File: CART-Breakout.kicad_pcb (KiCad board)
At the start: 2 copper layers, 47 x 50 mm, 11 parts, among them P1 CONN_01X05, P2 CONN_01X05, P3 CONN_01X05, P4 CONN_01X05, P5 CONN_01X05, P6 CONN_01X05

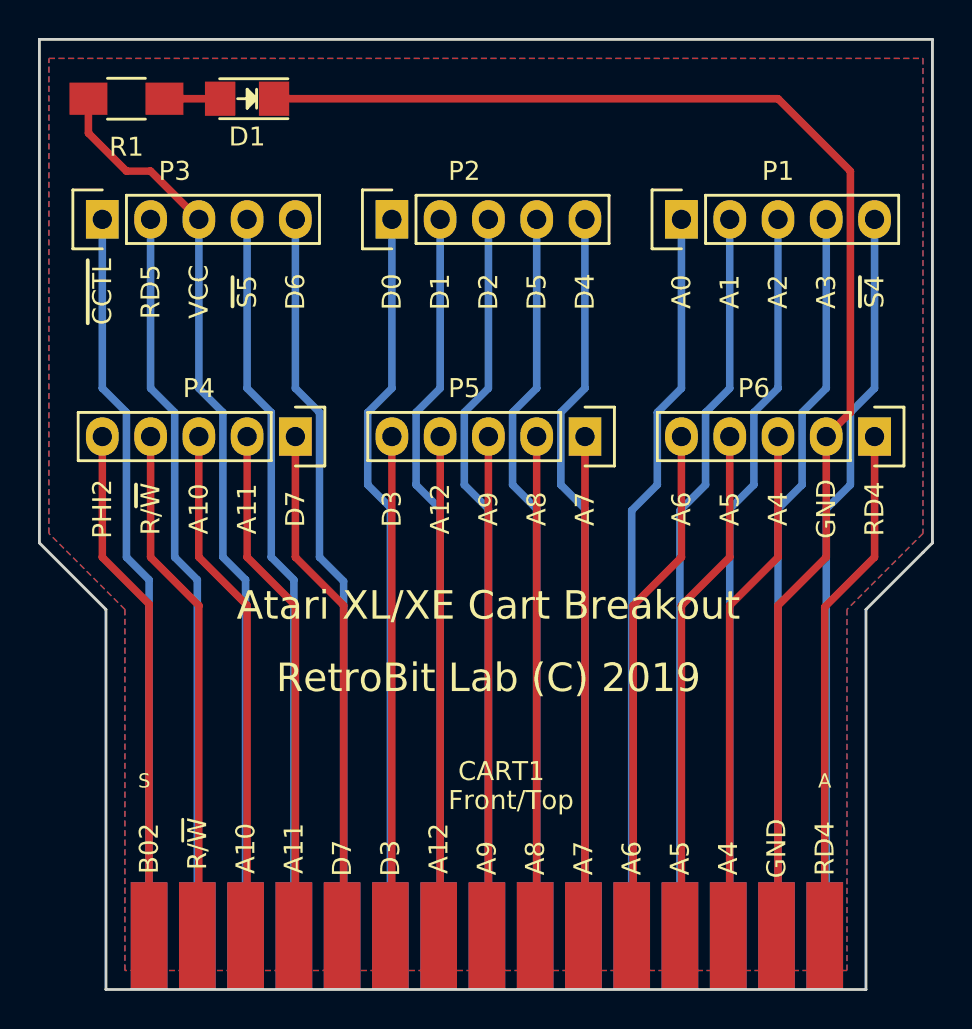
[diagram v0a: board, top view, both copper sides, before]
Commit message: Updated from KiCAD 4 to KiCAD 5.1.19
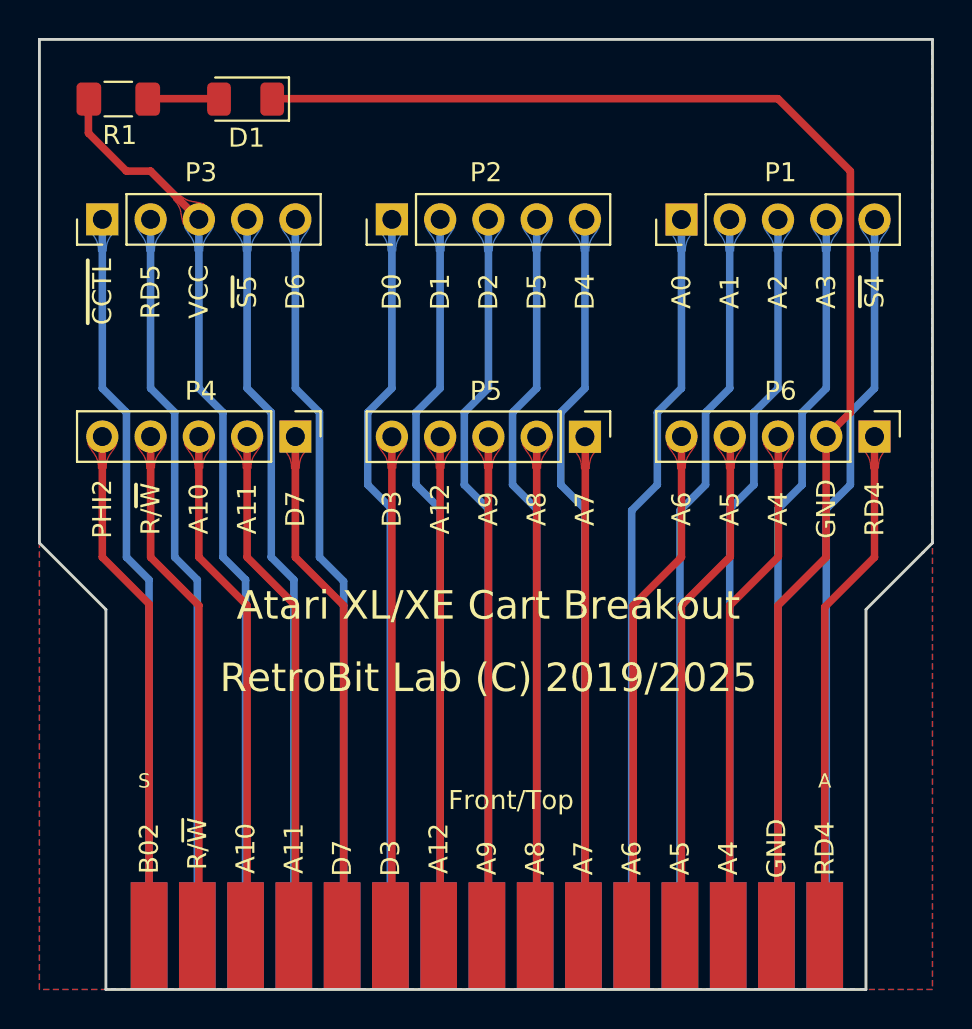
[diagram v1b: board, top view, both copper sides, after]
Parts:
- removed LOGO: KiCad-Logo_5mm_SilkScreen, Symbol:KiCad-Logo_5mm_SilkScreen
- removed OSHW: OSHW-Logo_5.7x6mm_SilkScreen, Symbol:OSHW-Logo_5.7x6mm_SilkScreen
- added L1: LOGO, Symbol:OSHW-Logo2_7.3x6mm_SilkScreen, B.Cu at (151.5, 104.0)
- added L2: LOGO, Symbol:KiCad-Logo2_5mm_SilkScreen, B.Cu at (151.0, 97.5)
- D1: footprint LEDs:LED_1206 -> LED_SMD:LED_1206_3216Metric
- P1, P2, P3, P4, P5, P6: value CONN_01X05 -> Conn_01x05; footprint Pin_Headers:Pin_Header_Straight_1x05 -> Connector_PinHeader_2.54mm:PinHeader_1x05_P2.54mm_Vertical
- R1: footprint Resistors_SMD:R_1206_HandSoldering -> Resistor_SMD:R_1206_3216Metric_Pad1.30x1.75mm_HandSolder
- moved R1 0.43 mm to (131.7, 71.1)
- moved D1 0.08 mm to (138.3, 71.1)
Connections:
- net Net-(CART1-Pad1) renamed /~S4
- net Net-(CART1-Pad10) renamed /D0
- net Net-(CART1-Pad11) renamed /D6
- net Net-(CART1-Pad12) renamed /~S5
- net Net-(CART1-Pad14) renamed /RD5
- net Net-(CART1-Pad15) renamed /~CCTL
- net Net-(CART1-Pad2) renamed /A3
- net Net-(CART1-Pad3) renamed /A2
- net Net-(CART1-Pad4) renamed /A1
- net Net-(CART1-Pad5) renamed /A0
- net Net-(CART1-Pad6) renamed /D4
- net Net-(CART1-Pad7) renamed /D5
- net Net-(CART1-Pad8) renamed /D2
- net Net-(CART1-Pad9) renamed /D1
- net Net-(CART1-PadA) renamed /RD4
- net Net-(CART1-PadC) renamed /A4
- net Net-(CART1-PadD) renamed /A5
- net Net-(CART1-PadE) renamed /A6
- net Net-(CART1-PadF) renamed /A7
- net Net-(CART1-PadH) renamed /A8
- net Net-(CART1-PadJ) renamed /A9
- net Net-(CART1-PadK) renamed /A12
- net Net-(CART1-PadL) renamed /D3
- net Net-(CART1-PadM) renamed /D7
- net Net-(CART1-PadN) renamed /A11
- net Net-(CART1-PadP) renamed /A10
- net Net-(CART1-PadR) renamed /R~W
- net Net-(CART1-PadS) renamed /PHI2
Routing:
- net Net-(D1-Pad2): track 2.93 -> 3.82 mm
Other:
- board text added: "RetroBit Lab (C) 2019/2025"
- board text added: "in memoriam A.S.-G.D."
- board text removed: "RetroBit Lab (C) 2019"

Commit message: Migrate to KiCAD 9+
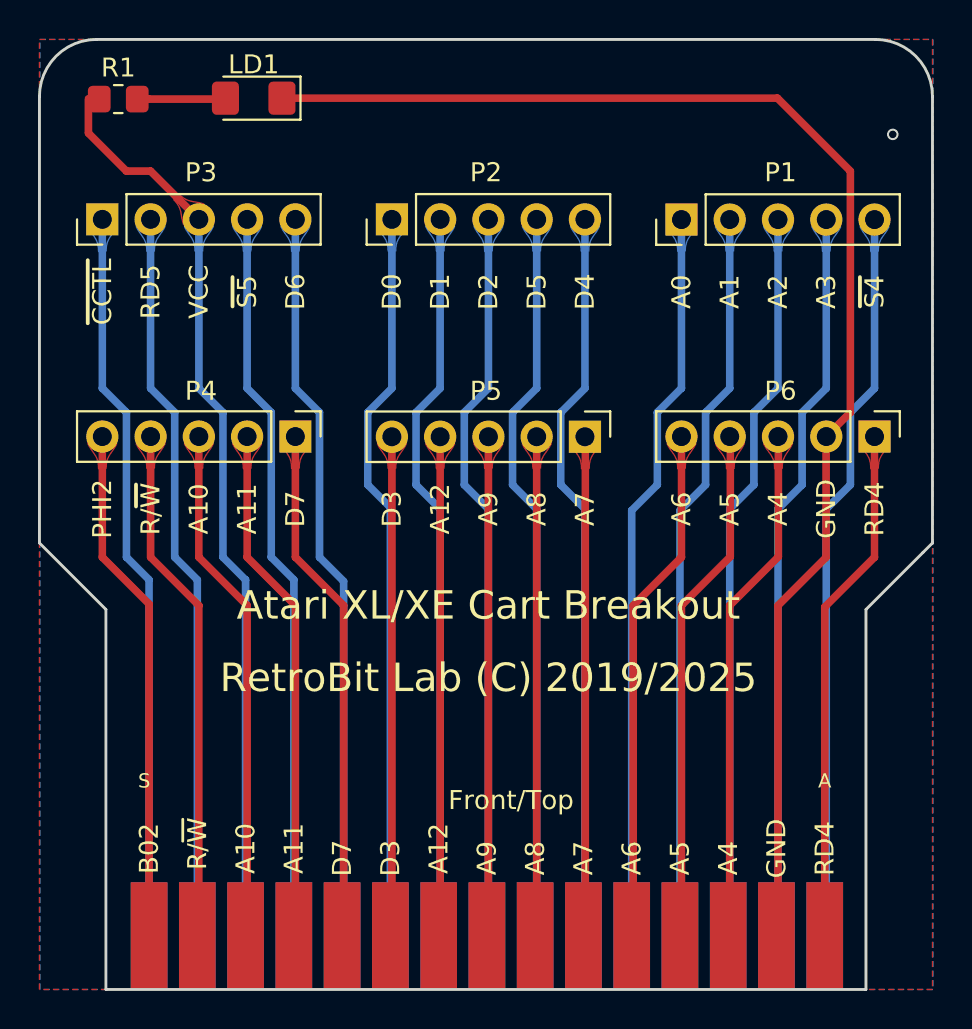
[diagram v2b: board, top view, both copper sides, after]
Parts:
- removed D1: YELLOW, LED_SMD:LED_1206_3216Metric
- added LD1: RED, LED_SMD:LED_1206_3216Metric_Pad1.42x1.75mm_HandSolder, F.Cu at (138.8, 71.1)
- R1: value 1.5K -> 1K; footprint Resistor_SMD:R_1206_3216Metric_Pad1.30x1.75mm_HandSolder -> Resistor_SMD:R_0805_2012Metric_Pad1.20x1.40mm_HandSolder
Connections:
- net /R~W renamed /R~{W}
- net /~CCTL renamed /~{CCTL}
- net /~S4 renamed /~{S4}
- net /~S5 renamed /~{S5}
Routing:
- net Net-(LD1-A): track 3.82 -> 4.69 mm
- net GND: track 73.7 -> 73.3 mm, vias 0 -> 1
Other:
- outline, holes or cut-outs redrawn
- net class Default removed
- board text added: "R/~{W}"
- board text added: "~{CCTL}"
- board text added: "~{S4}"
- board text added: "~{S5}"
- board text removed: "R/~W"
- board text removed: "~CCTL"
- board text removed: "~S4"
- board text removed: "~S5"
